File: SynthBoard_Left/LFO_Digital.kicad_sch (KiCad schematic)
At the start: 13 parts, among them IC3 PIC16F15325-I/SL, J2 ICSP LFO, U7 MCP6234T-E/SL

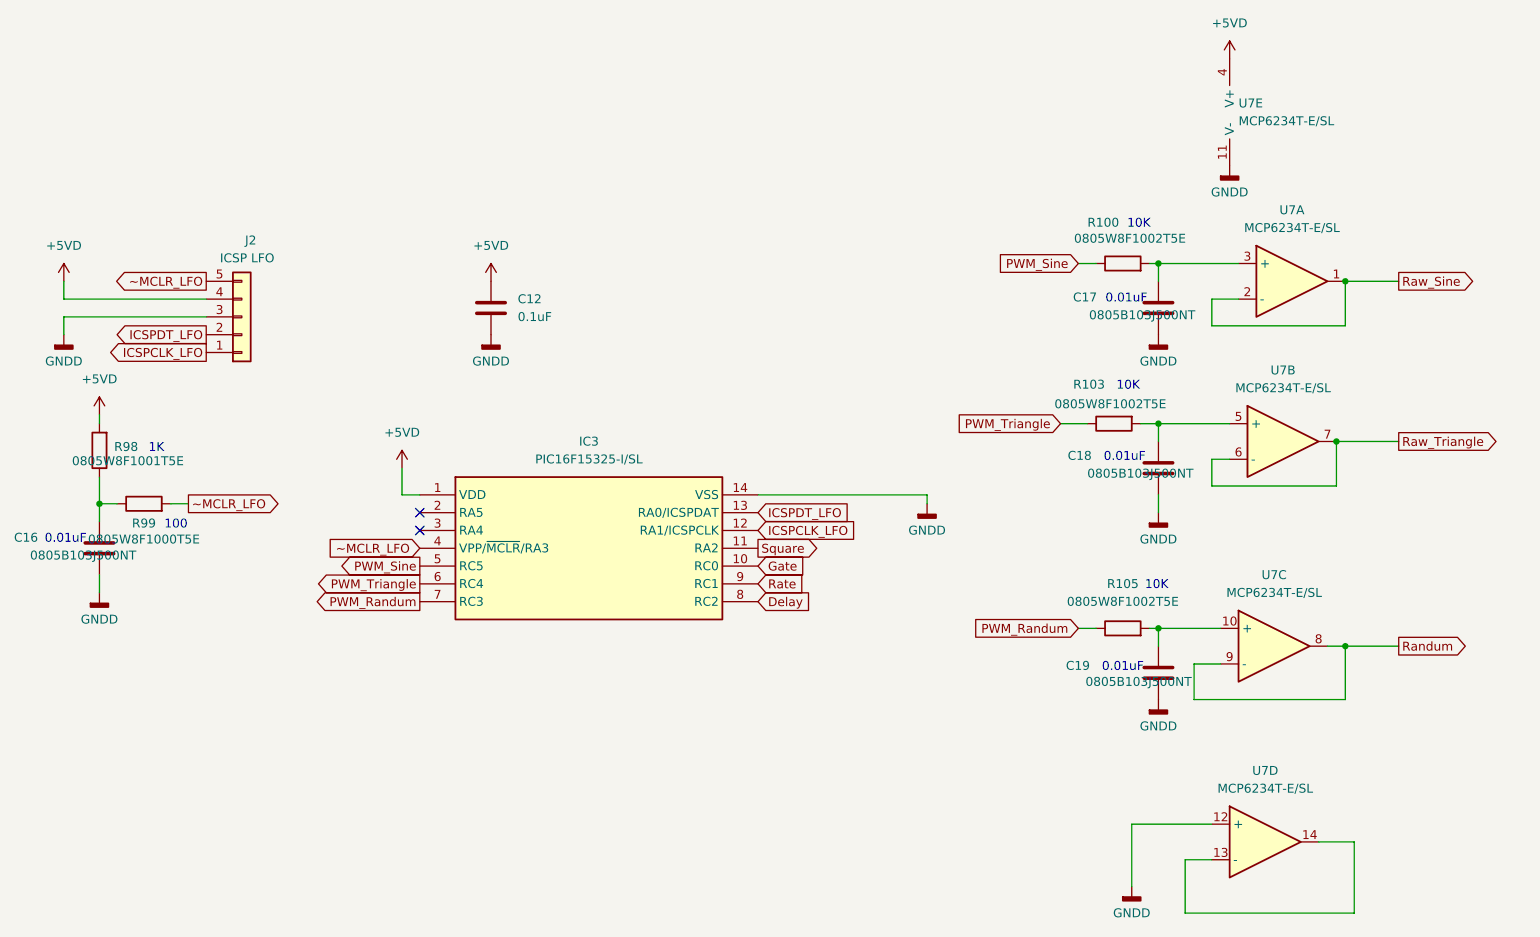
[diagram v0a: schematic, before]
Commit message: SynthBoard_Left
JLCPCBでBasic部品に置き換えた
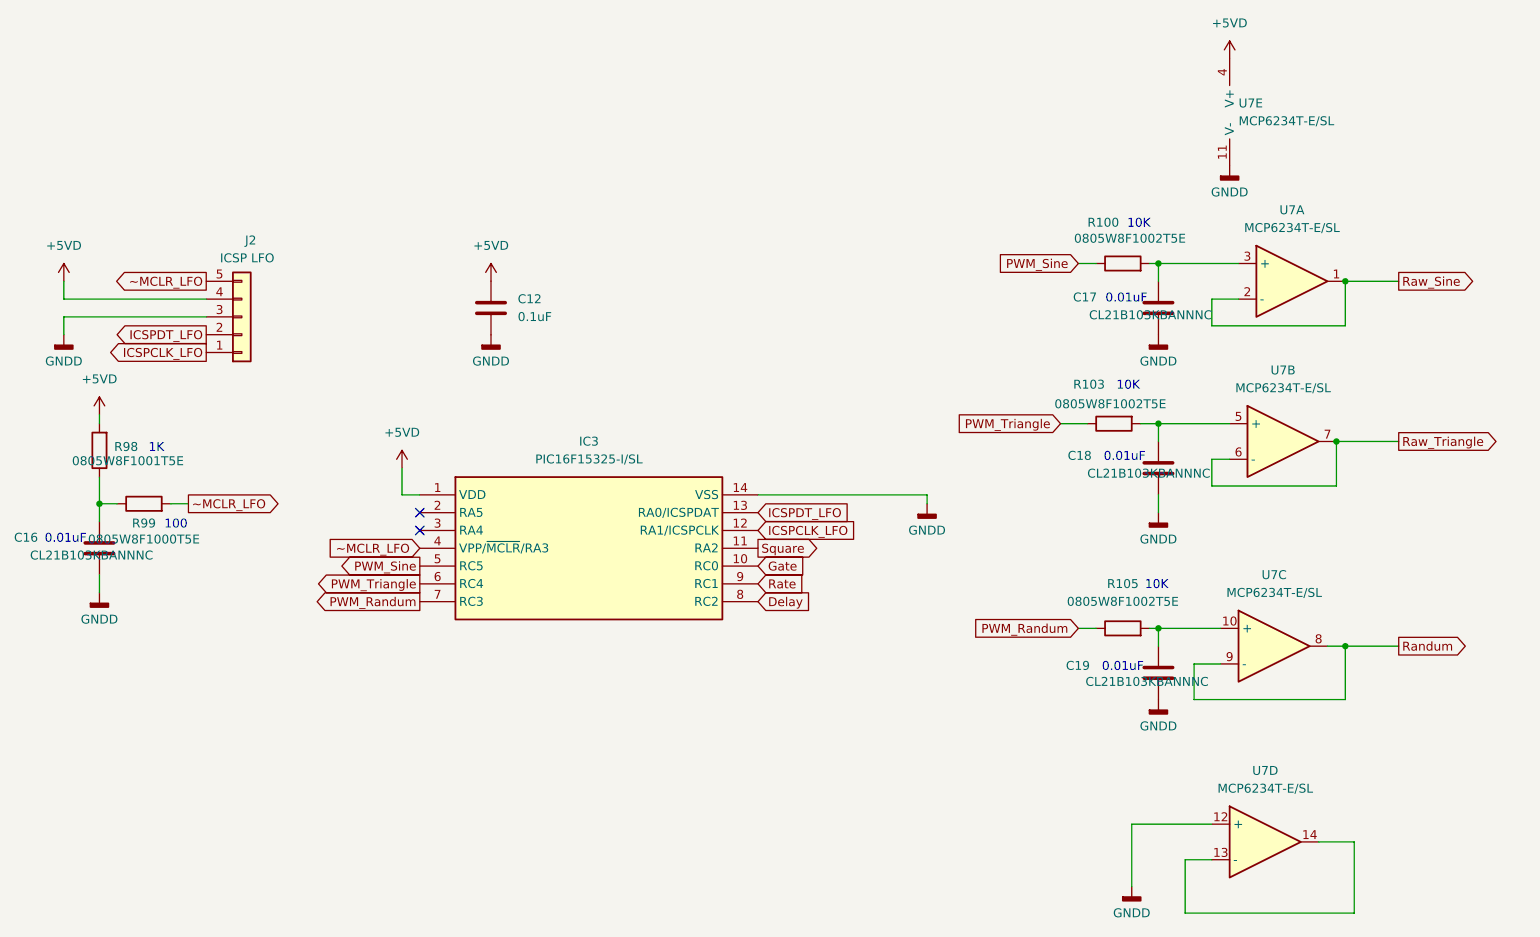
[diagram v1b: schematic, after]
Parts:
- C16, C17, C18, C19: value 0805B103J500NT -> CL21B103KBANNNC
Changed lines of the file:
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@@
 			)
 		)
-		(property "Value" "0805B103J500NT"
+		(property "Value" "CL21B103KBANNNC"
 			(at 201.93 82.042 0)
 			(effects
@@
 			)
 		)
-		(property "Value" "0805B103J500NT"
+		(property "Value" "CL21B103KBANNNC"
 			(at 51.054 93.726 0)
 			(effects
@@
 			)
 		)
-		(property "Value" "0805B103J500NT"
+		(property "Value" "CL21B103KBANNNC"
 			(at 202.184 59.436 0)
 			(effects
@@
 			)
 		)
-		(property "Value" "0805B103J500NT"
+		(property "Value" "CL21B103KBANNNC"
 			(at 201.676 111.76 0)
 			(effects

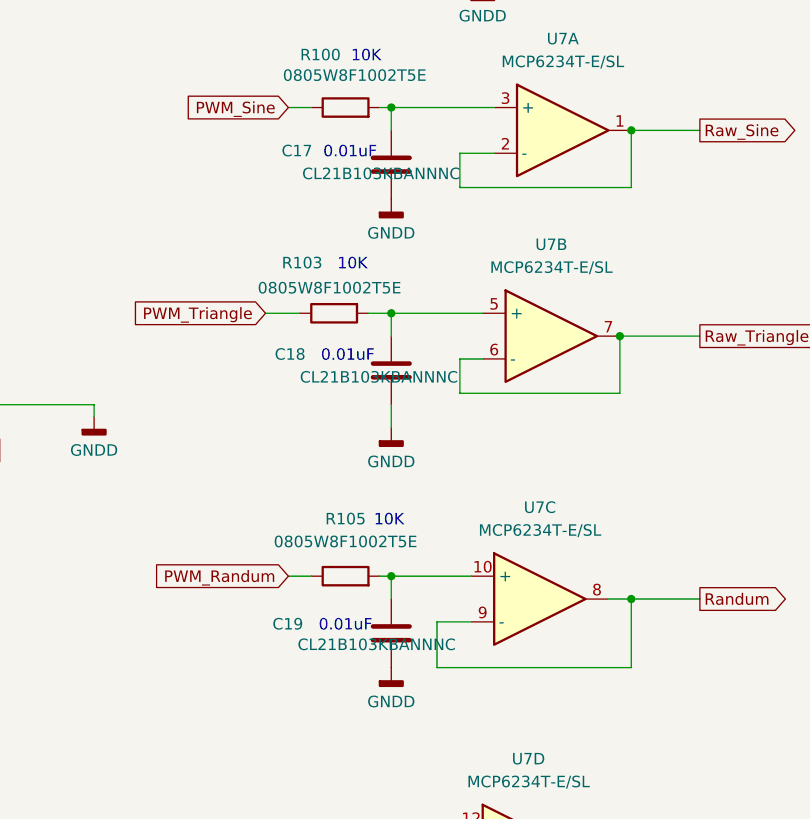
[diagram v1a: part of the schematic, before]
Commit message: MC2
まとめて登録
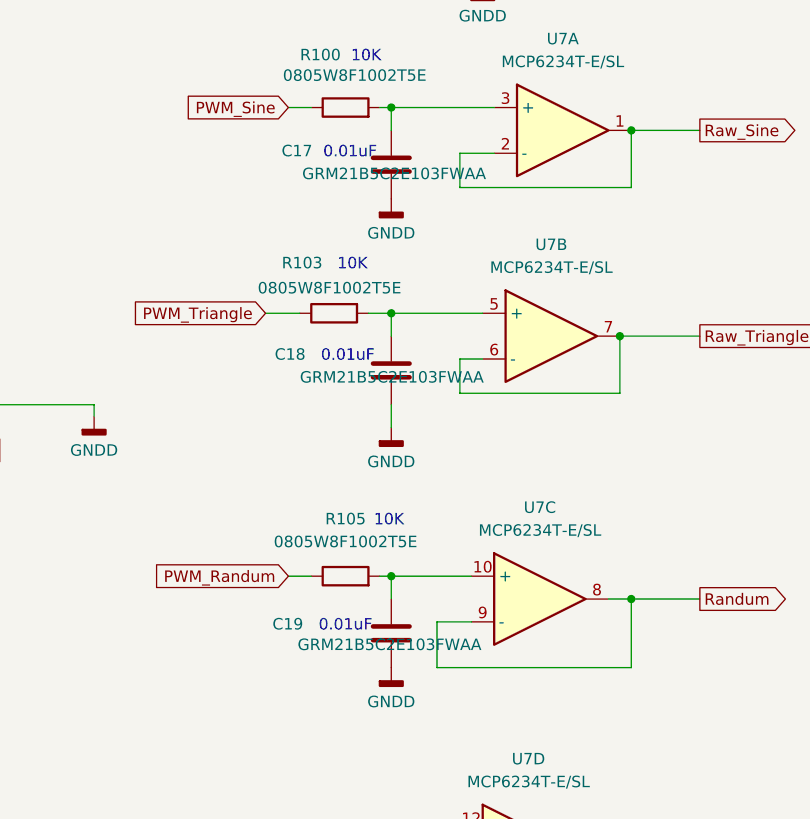
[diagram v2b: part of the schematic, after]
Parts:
- C17, C18, C19: value CL21B103KBANNNC -> GRM21B5C2E103FWAA
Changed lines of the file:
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@@
 			)
 		)
-		(property "Value" "CL21B103KBANNNC"
+		(property "Value" "GRM21B5C2E103FWAA"
 			(at 201.93 82.042 0)
 			(effects
@@
 			)
 		)
-		(property "Value" "CL21B103KBANNNC"
+		(property "Value" "GRM21B5C2E103FWAA"
 			(at 202.184 59.436 0)
 			(effects
@@
 			)
 		)
-		(property "Value" "CL21B103KBANNNC"
+		(property "Value" "GRM21B5C2E103FWAA"
 			(at 201.676 111.76 0)
 			(effects
